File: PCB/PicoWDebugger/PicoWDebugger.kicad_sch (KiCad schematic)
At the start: 10 parts, among them J1 External_Connections, J2 SWD, SW1 UART, SW2 Reset_Target

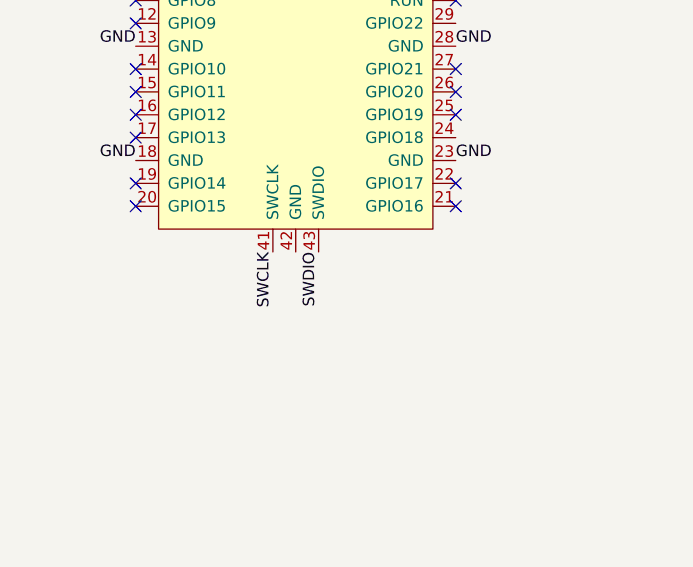
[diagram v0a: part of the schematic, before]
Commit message: Updated design, added PicoW version
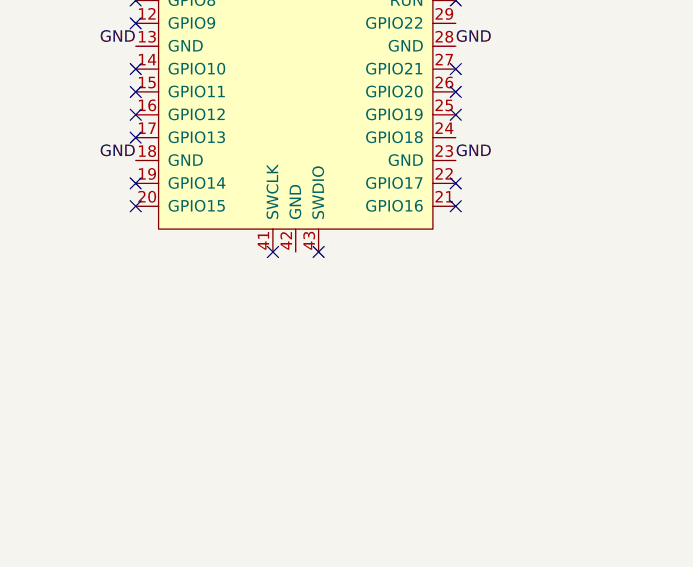
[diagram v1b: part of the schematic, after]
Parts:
- Target1: footprint MCU_RaspberryPi_and_Boards:RPi_Pico_SMD_TH -> MCU_RaspberryPi_and_Boards:RPi_Pico_W_SMD_TH
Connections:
- net SWCLK: no longer PicoProbe1.41 (SWCLK)
- net SWDIO: no longer PicoProbe1.43 (SWDIO)
- no-connect marks 24 -> 26
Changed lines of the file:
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@@
   (no_connect (at 87.63 80.01))
   (no_connect (at 87.63 62.23))
+  (no_connect (at 67.31 95.25))
   (no_connect (at 87.63 87.63))
   (no_connect (at 52.07 74.93))
+  (no_connect (at 72.39 95.25))
   (no_connect (at 52.07 69.85))
   (no_connect (at 52.07 80.01))
@@
     (effects (font (size 1.27 1.27)) (justify left bottom))
   )
-  (label "SWDIO" (at 72.39 95.25 270) (fields_autoplaced)
-    (effects (font (size 1.27 1.27)) (justify right bottom))
-  )
   (label "TT_UART_Rx" (at 198.12 46.99 180) (fields_autoplaced)
     (effects (font (size 1.27 1.27)) (justify right bottom))
@@
     (effects (font (size 1.27 1.27)) (justify left bottom))
   )
-  (label "SWCLK" (at 67.31 95.25 270) (fields_autoplaced)
-    (effects (font (size 1.27 1.27)) (justify right bottom))
-  )
   (label "TT_UART_Tx" (at 127 43.18 180) (fields_autoplaced)
     (effects (font (size 1.27 1.27)) (justify right bottom))
@@
     (pin "2")
     (instances
-      (project "PicoprobeTester"
+      (project "PicoWDebugger"
         (path "/32bb4d5c-5047-40f3-b26d-b1a75322ad60"
           (reference "SW2") (unit 1)
@@
     (pin "9")
     (instances
-      (project "PicoprobeTester"
+      (project "PicoWDebugger"
         (path "/32bb4d5c-5047-40f3-b26d-b1a75322ad60"
           (reference "J1") (unit 1)
@@
     )
     (instances
-      (project "PicoprobeTester"
+      (project "PicoWDebugger"
         (path "/32bb4d5c-5047-40f3-b26d-b1a75322ad60"
           (reference "H4") (unit 1)
@@
       (effects (font (size 1.27 1.27)))
     )
-    (property "Footprint" "MCU_RaspberryPi_and_Boards:RPi_Pico_SMD_TH" (at 144.78 67.31 90)
+    (property "Footprint" "MCU_RaspberryPi_and_Boards:RPi_Pico_W_SMD_TH" (at 144.78 67.31 90)
       (effects (font (size 1.27 1.27)) hide)
     )
@@
     (pin "9")
     (instances
-      (project "PicoprobeTester"
+      (project "PicoWDebugger"
         (path "/32bb4d5c-5047-40f3-b26d-b1a75322ad60"
           (reference "Target1") (unit 1)
@@
     (pin "3")
     (instances
-      (project "PicoprobeTester"
+      (project "PicoWDebugger"
         (path "/32bb4d5c-5047-40f3-b26d-b1a75322ad60"
           (reference "J2") (unit 1)
@@
     (pin "1")
     (instances
-      (project "PicoprobeTester"
+      (project "PicoWDebugger"
         (path "/32bb4d5c-5047-40f3-b26d-b1a75322ad60"
           (reference "#FLG01") (unit 1)
@@
     (pin "9")
     (instances
-      (project "PicoprobeTester"
+      (project "PicoWDebugger"
         (path "/32bb4d5c-5047-40f3-b26d-b1a75322ad60"
           (reference "PicoProbe1") (unit 1)
@@
     (pin "1")
     (instances
-      (project "PicoprobeTester"
+      (project "PicoWDebugger"
         (path "/32bb4d5c-5047-40f3-b26d-b1a75322ad60"
           (reference "#PWR01") (unit 1)
@@
     )
     (instances
-      (project "PicoprobeTester"
+      (project "PicoWDebugger"
         (path "/32bb4d5c-5047-40f3-b26d-b1a75322ad60"
           (reference "H3") (unit 1)
@@
     (pin "4")
     (instances
-      (project "PicoprobeTester"
+      (project "PicoWDebugger"
         (path "/32bb4d5c-5047-40f3-b26d-b1a75322ad60"
           (reference "SW1") (unit 1)
@@
     (pin "1")
     (instances
-      (project "PicoprobeTester"
+      (project "PicoWDebugger"
         (path "/32bb4d5c-5047-40f3-b26d-b1a75322ad60"
           (reference "#FLG02") (unit 1)
@@
     (pin "1")
     (instances
-      (project "PicoprobeTester"
+      (project "PicoWDebugger"
         (path "/32bb4d5c-5047-40f3-b26d-b1a75322ad60"
           (reference "#PWR02") (unit 1)
@@
     )
     (instances
-      (project "PicoprobeTester"
+      (project "PicoWDebugger"
         (path "/32bb4d5c-5047-40f3-b26d-b1a75322ad60"
           (reference "H2") (unit 1)
@@
     )
     (instances
-      (project "PicoprobeTester"
+      (project "PicoWDebugger"
         (path "/32bb4d5c-5047-40f3-b26d-b1a75322ad60"
           (reference "H1") (unit 1)
